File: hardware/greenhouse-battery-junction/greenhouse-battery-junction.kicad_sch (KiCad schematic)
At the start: 23 parts, among them J1 Conn_01x10_Female, J10 Conn_01x03_Female, J11 Screw_Terminal_01x02, J12 Conn_01x04_Male, J2 Conn_01x03_Female

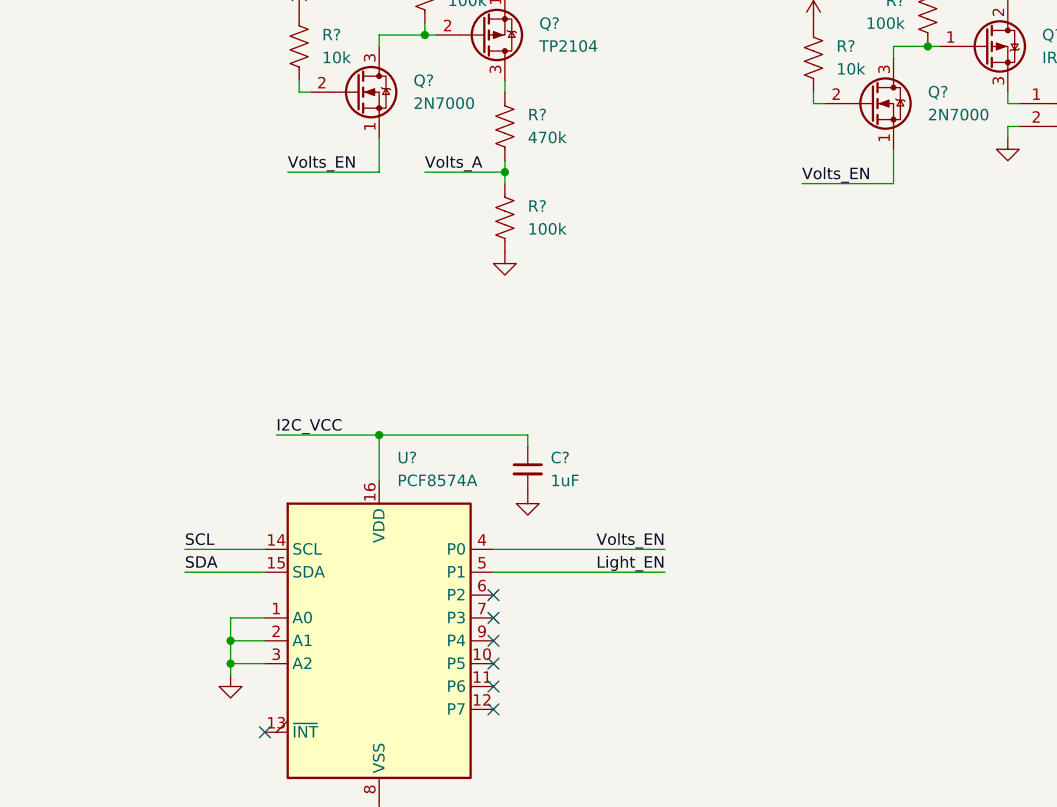
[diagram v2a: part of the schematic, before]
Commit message: Set PCF addr to 0x21
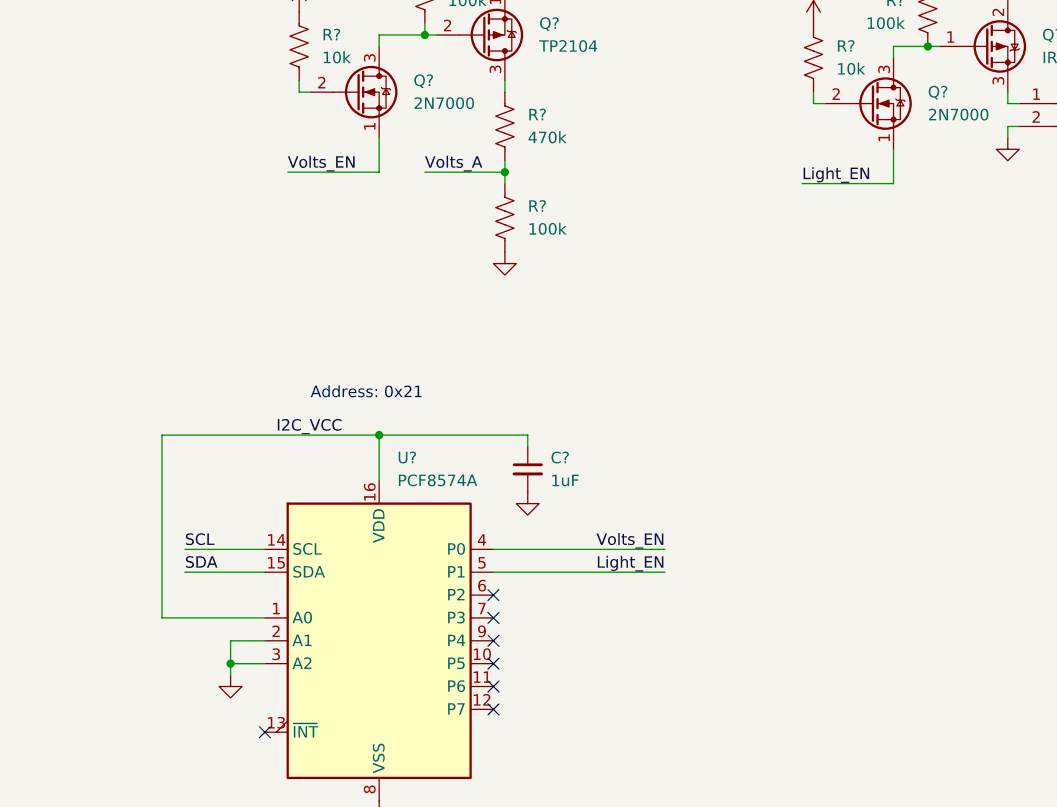
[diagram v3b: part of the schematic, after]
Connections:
- net +3V3: now also U?.1 (A0)
- net GND: no longer U?.1 (A0)
- net Light_EN: now also Q?.1 (S)
- net Volts_EN: no longer Q?.1 (S)
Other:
- note added: "Address: 0x21"
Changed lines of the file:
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@@
   (junction (at 173.99 40.64) (diameter 0) (color 0 0 0 0)
-  )
-  (junction (at 152.4 107.95) (diameter 0) (color 0 0 0 0)
   )
   (junction (at 182.88 55.88) (diameter 0) (color 0 0 0 0)
@@
     (stroke (width 0) (type default) (color 0 0 0 0))
   )
-  (wire (pts (xy 157.48 85.09) (xy 168.91 85.09))
+  (wire (pts (xy 144.78 85.09) (xy 168.91 85.09))
     (stroke (width 0) (type default) (color 0 0 0 0))
   )
@@
     (stroke (width 0) (type default) (color 0 0 0 0))
   )
-  (wire (pts (xy 152.4 105.41) (xy 152.4 107.95))
-    (stroke (width 0) (type default) (color 0 0 0 0))
-  )
   (wire (pts (xy 88.9 115.57) (xy 88.9 156.21))
     (stroke (width 0) (type default) (color 0 0 0 0))
@@
     (stroke (width 0) (type default) (color 0 0 0 0))
   )
-  (wire (pts (xy 156.21 105.41) (xy 152.4 105.41))
+  (wire (pts (xy 144.78 105.41) (xy 156.21 105.41))
     (stroke (width 0) (type default) (color 0 0 0 0))
   )
@@
     (stroke (width 0) (type default) (color 0 0 0 0))
   )
+  (wire (pts (xy 144.78 85.09) (xy 144.78 105.41))
+    (stroke (width 0) (type default) (color 0 0 0 0))
+  )
   (wire (pts (xy 60.96 45.72) (xy 76.2 45.72))
     (stroke (width 0) (type default) (color 0 0 0 0))
@@
     (effects (font (size 1.27 1.27)) (justify left bottom))
   )
+  (text "Address: 0x21 " (at 161.29 81.28 0)
+    (effects (font (size 1.27 1.27)) (justify left bottom))
+  )
   (text "Common gate protects \nIO IC (max 3.3 V)" (at 149.86 30.48 0)
     (effects (font (size 1.27 1.27)) (justify left bottom))
@@
     (effects (font (size 1.27 1.27)) (justify left bottom))
   )
-  (label "Volts_EN" (at 215.9 57.15 0)
-    (effects (font (size 1.27 1.27)) (justify left bottom))
-  )
   (label "Volts_A" (at 173.99 55.88 0)
     (effects (font (size 1.27 1.27)) (justify left bottom))
@@
     (effects (font (size 1.27 1.27)) (justify right bottom))
   )
+  (label "Light_EN" (at 215.9 57.15 0)
+    (effects (font (size 1.27 1.27)) (justify left bottom))
+  )
   (label "Current_A" (at 85.09 143.51 180)

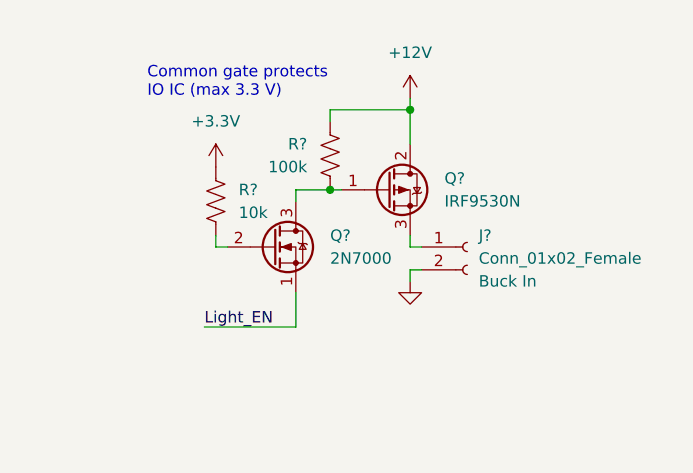
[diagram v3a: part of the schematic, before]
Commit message: Fix FET orientation
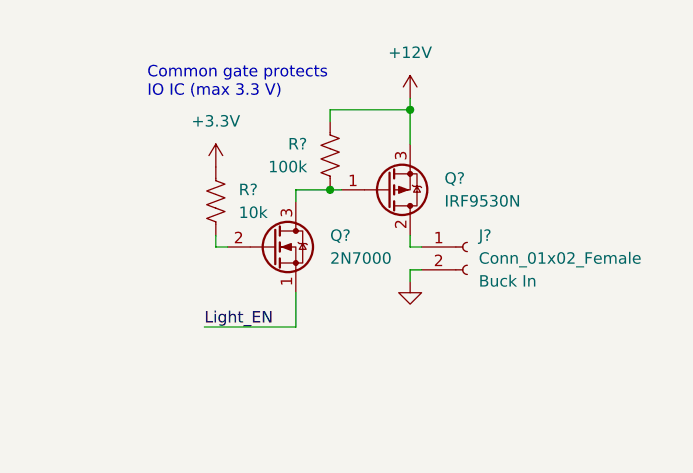
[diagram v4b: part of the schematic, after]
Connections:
- net +12V: now also Q?.3 (S); no longer Q?.2 (D)
- net at J?.1 (Pin_1): now also Q?.2 (D); no longer Q?.3 (S)
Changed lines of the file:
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@@
     (pin "1")
   )
-  (symbol (lib_id "Transistor_FET:IRF9540N") (at 236.22 41.91 0) (unit 1)
+  (symbol (lib_id "Transistor_FET:IRF9540N") (at 236.22 41.91 0) (mirror x) (unit 1)
     (in_bom yes) (on_board yes) (fields_autoplaced)
     (property "Reference" "Q?" (id 0) (at 242.57 40.6399 0)
@@
       (effects (font (size 1.27 1.27)) (justify left))
     )
-    (property "Footprint" "Package_TO_SOT_THT:TO-220-3_Vertical" (id 2) (at 241.3 43.815 0)
+    (property "Footprint" "Package_TO_SOT_THT:TO-220-3_Vertical" (id 2) (at 241.3 40.005 0)
       (effects (font (size 1.27 1.27) italic) (justify left) hide)
     )

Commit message: First pass at R4
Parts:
- removed Q?: TP2104, Package_TO_SOT_THT:TO-92_Inline, symbol Device:Q_PMOS_SGD
- removed Q?: 2N7000, Package_TO_SOT_THT:TO-92_Inline, symbol Transistor_FET:2N7000
- removed R?: 10k, symbol Device:R_US
- removed R?: 100k, symbol Device:R_US
- R?: value 100k -> 47k
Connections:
- net +12V: now also R?.1
- net Volts_EN: no longer names the net of U?.4 (P0)
- no-connect marks 12 -> 13
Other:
- moved on the sheet: R?

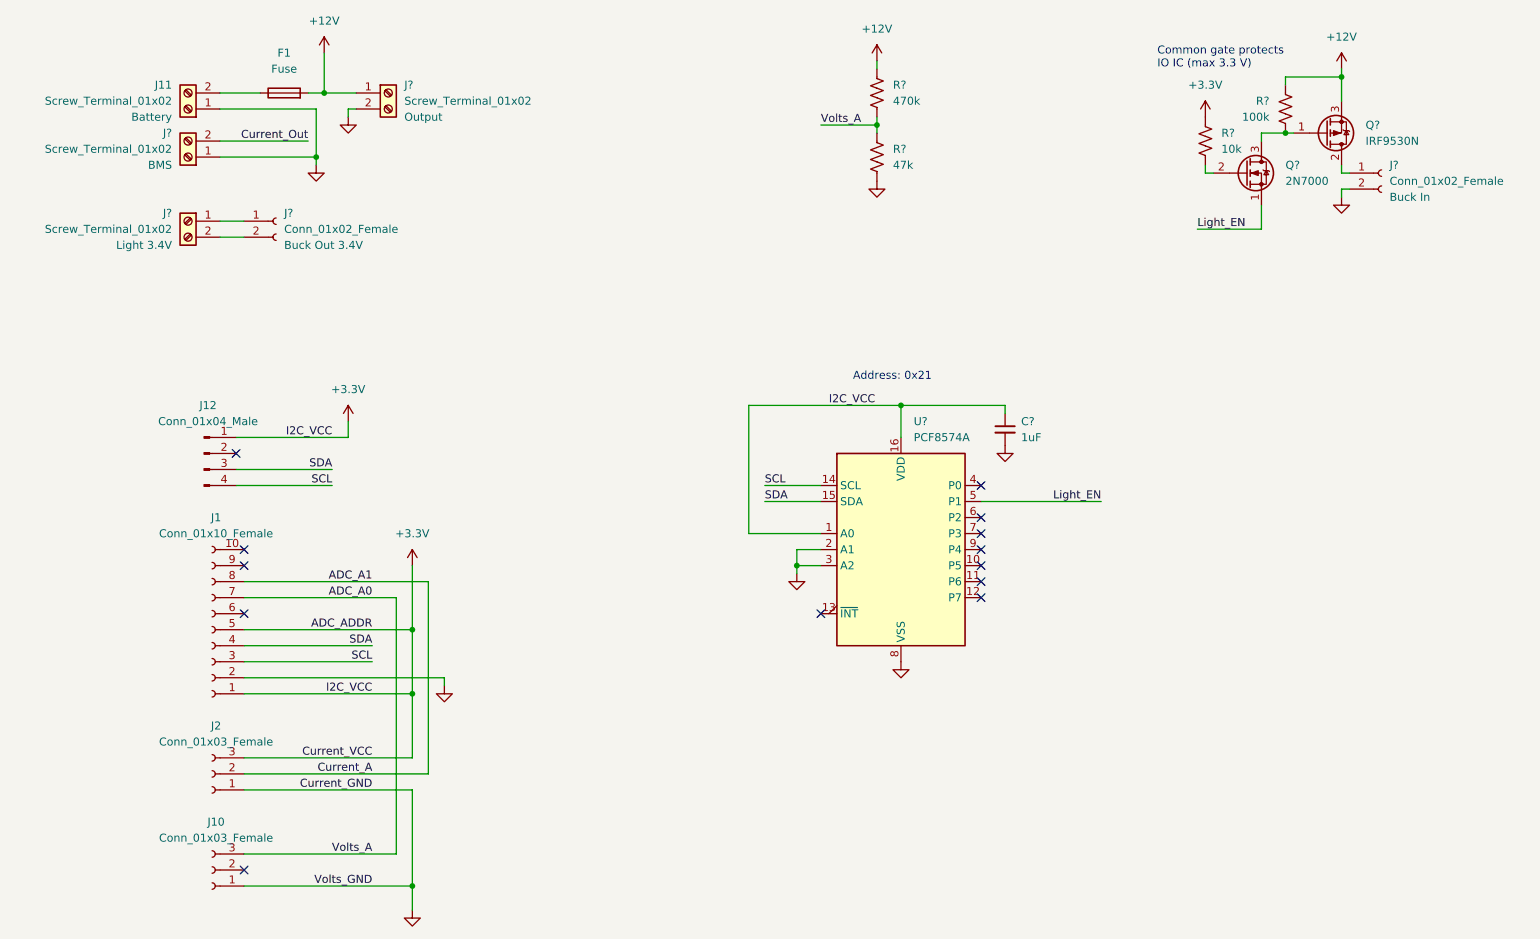
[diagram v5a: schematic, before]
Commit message: Improved GND loop for battery ADC
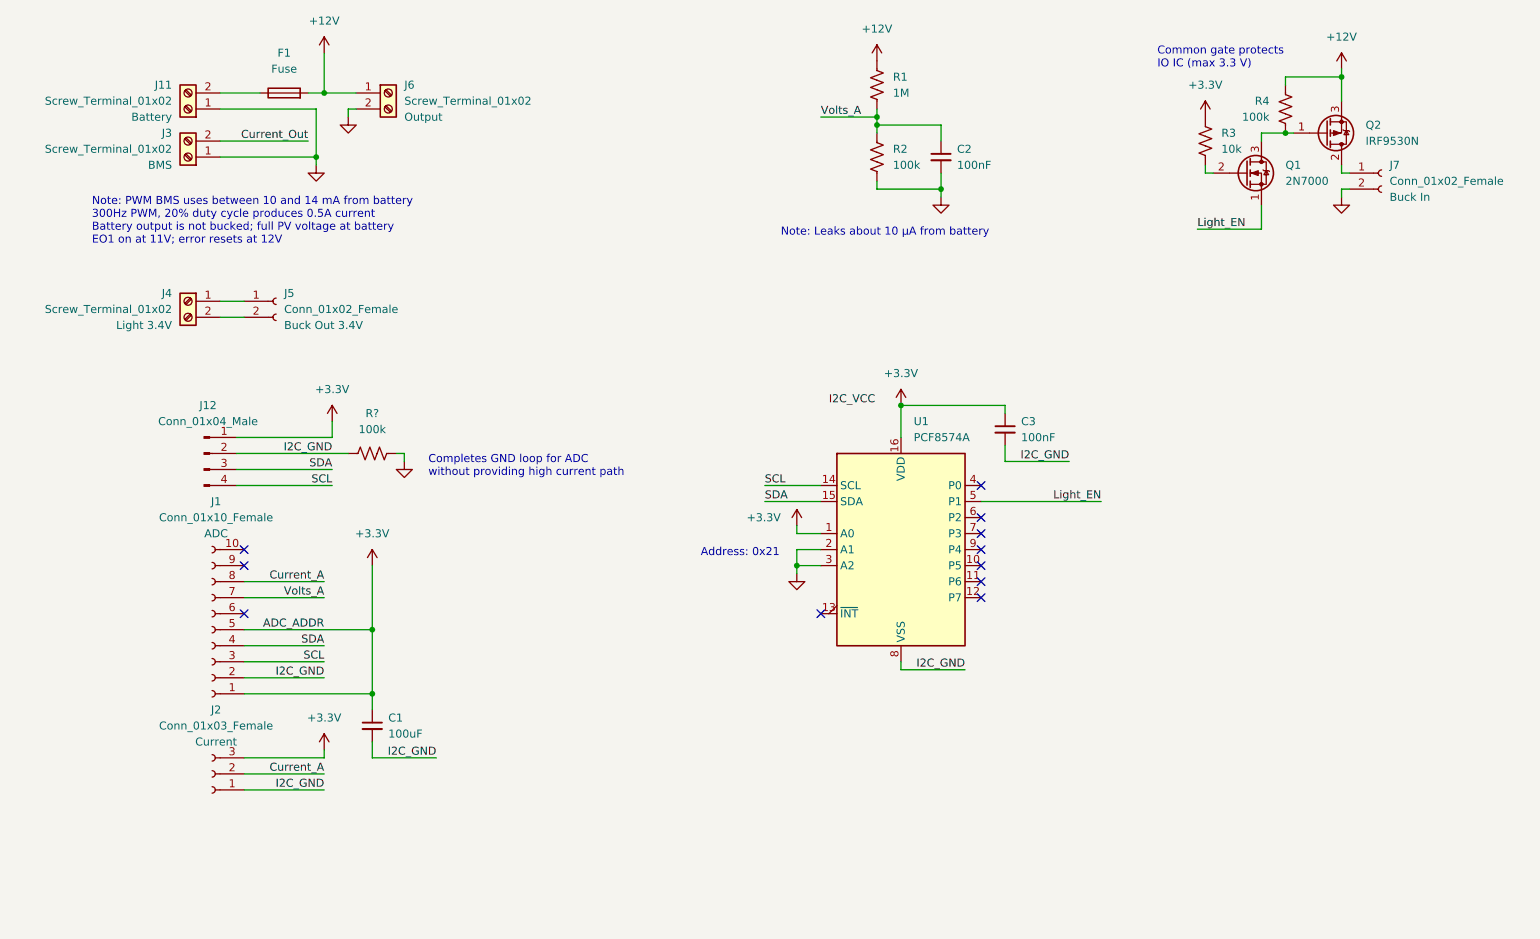
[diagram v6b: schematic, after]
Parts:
- removed J10: Conn_01x03_Female, Connector_PinHeader_2.54mm:PinHeader_1x03_P2.54mm_Vertical, symbol Connector:Conn_01x03_Female
- added C1: 100uF, symbol Device:C_Small
- added C2: 100nF, symbol Device:C_Small
- added R?: 100k, symbol Device:R_US
- C3: renamed from C?; value 1uF -> 100nF
- J1: Module (none) -> ADC
- J2: Module (none) -> Current
- R1: renamed from R?; value 470k -> 1M
- R2: renamed from R?; value 47k -> 100k
- gave numbers to parts that had none: 10
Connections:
- net +3V3: now also C1.1
- net GND: now also C2.2, R?.2; no longer C3.2, J1.2 (Pin_2), J2.1 (Pin_1), U1.8 (VSS)
- net I2C_GND: now reaches J12.2 (Pin_2)
- net I2C_GND: now also C3.2, J1.2 (Pin_2), J2.1 (Pin_1), U1.8 (VSS), C1.2, R?.1
- net ADC_A0 renamed Volts_A
- net Volts_A: now also C2.1
- net ADC_A1 renamed Current_A
- no-connect marks 13 -> 11
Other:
- note added: "Completes GND loop for ADC without providing high current path"
- note added: "Note: Leaks about 10 μA from battery"
- note added: "Note: PWM BMS uses between 10 and 14 mA from battery 300Hz PWM, 20% duty cycle produces 0.5A current Battery output is not bucked; full PV voltage at battery EO1 on at 11V; error resets at 12V"
- moved on the sheet: J4, J5, R1

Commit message: Remove I2C GND connection
Use main GND connection instead
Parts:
- removed R?: 100k, symbol Device:R_US
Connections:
- net GND: now also C1.2, C3.2, J1.2 (Pin_2), J2.1 (Pin_1), U1.8 (VSS)
- removed net I2C_GND: C1.2, C3.2, J1.2 (Pin_2), J12.2 (Pin_2), J2.1 (Pin_1), U1.8 (VSS)
- no-connect marks 11 -> 12
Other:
- note added: "Note: Do not use GND on the I2C header, as this provides a return current path for loads; I2C GND works fine via main GND"
- note removed: "Completes GND loop for ADC without providing high current path"
